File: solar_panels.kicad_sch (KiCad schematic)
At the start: 2 parts, among them J2 Conn_01x02_Pin, J3 Conn_01x02_Pin

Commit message: BOM in folder
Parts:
- J2, J3: Supplier_1 (none) -> LCSC; Supplier_1 P/N (none) -> C431092
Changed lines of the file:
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@@
 			)
 		)
-		(property "Supplier_1" ""
-			(at 99.06 95.25 0)
-			(effects
-				(font
-					(size 1.27 1.27)
-				)
-				(hide yes)
-			)
-		)
-		(property "Supplier_1 P/N" ""
+		(property "Supplier_1" "LCSC"
+			(at 99.06 95.25 0)
+			(effects
+				(font
+					(size 1.27 1.27)
+				)
+				(hide yes)
+			)
+		)
+		(property "Supplier_1 P/N" "C431092"
 			(at 99.06 95.25 0)
 			(effects
@@
 		)
 		(property "Supplier_2 Price @ Qty" ""
+			(at 99.06 95.25 0)
+			(effects
+				(font
+					(size 1.27 1.27)
+				)
+				(hide yes)
+			)
+		)
+		(property "SNAPEDA_PN" ""
 			(at 99.06 95.25 0)
 			(effects
@@
 			)
 		)
-		(property "Supplier_1" ""
-			(at 99.06 78.74 0)
-			(effects
-				(font
-					(size 1.27 1.27)
-				)
-				(hide yes)
-			)
-		)
-		(property "Supplier_1 P/N" ""
+		(property "Supplier_1" "LCSC"
+			(at 99.06 78.74 0)
+			(effects
+				(font
+					(size 1.27 1.27)
+				)
+				(hide yes)
+			)
+		)
+		(property "Supplier_1 P/N" "C431092"
 			(at 99.06 78.74 0)
 			(effects
@@
 			(at 99.06 78.74 0)
 			(effects
+				(font
+					(size 1.27 1.27)
+				)
+				(hide yes)
+			)
+		)
+		(property "SNAPEDA_PN" ""
+			(at 99.06 78.74 0)
+			(effects

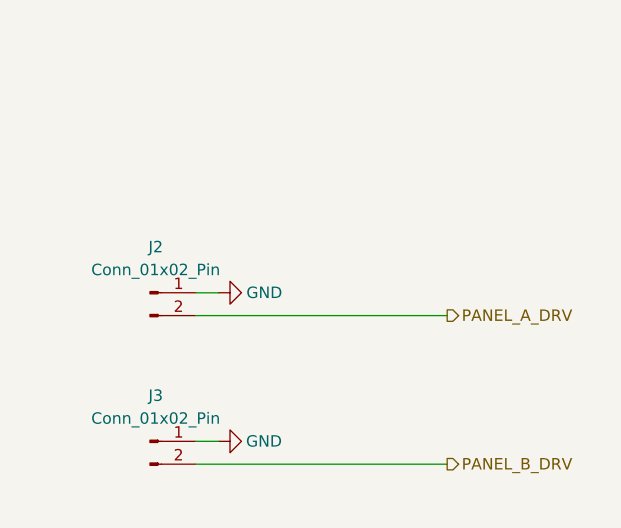
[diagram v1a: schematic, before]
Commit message: Schematic updates
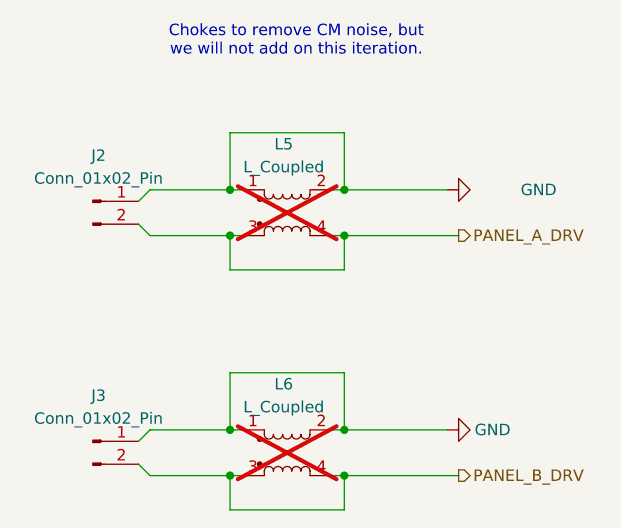
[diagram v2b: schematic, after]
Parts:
- added L5, L6: L_Coupled, symbol Device:L_Coupled
- J2: Mfr (none) -> Changzhou Amass Elec; Mfr P/N (none) -> XT30PW-M30.G.Y
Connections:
- net GND: now also L5.1, L5.2, L6.1, L6.2
- net PANEL_A_DRV: now also L5.3, L5.4
- net PANEL_B_DRV: now also L6.3, L6.4
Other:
- note added: "Chokes to remove CM noise, but we will not add on this iteration."
- moved on the sheet: J2, J3
